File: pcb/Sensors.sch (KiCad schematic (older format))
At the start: 6 parts, among them U1 MPL3115A2, U13 HTS221

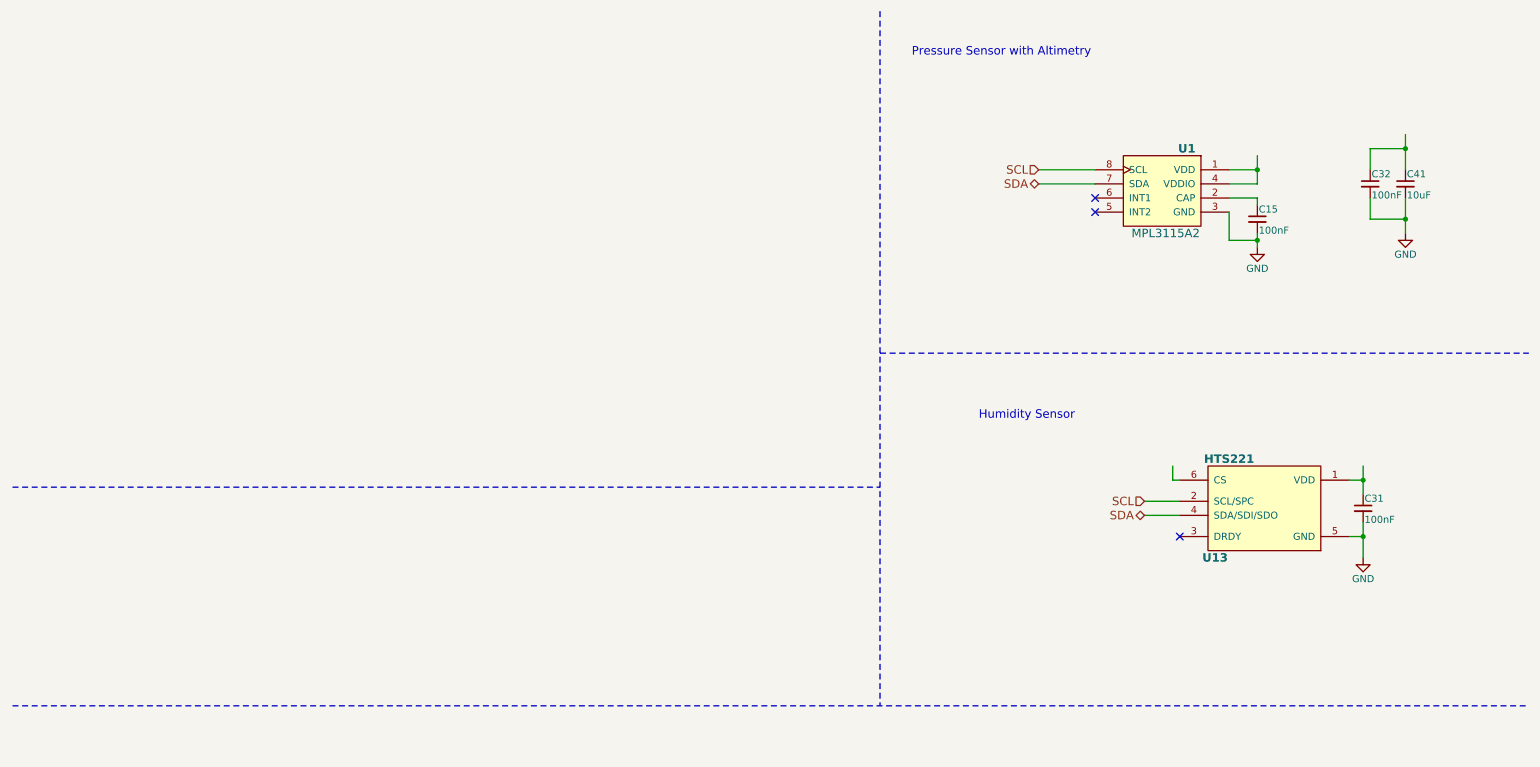
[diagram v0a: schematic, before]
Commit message: sensor array started
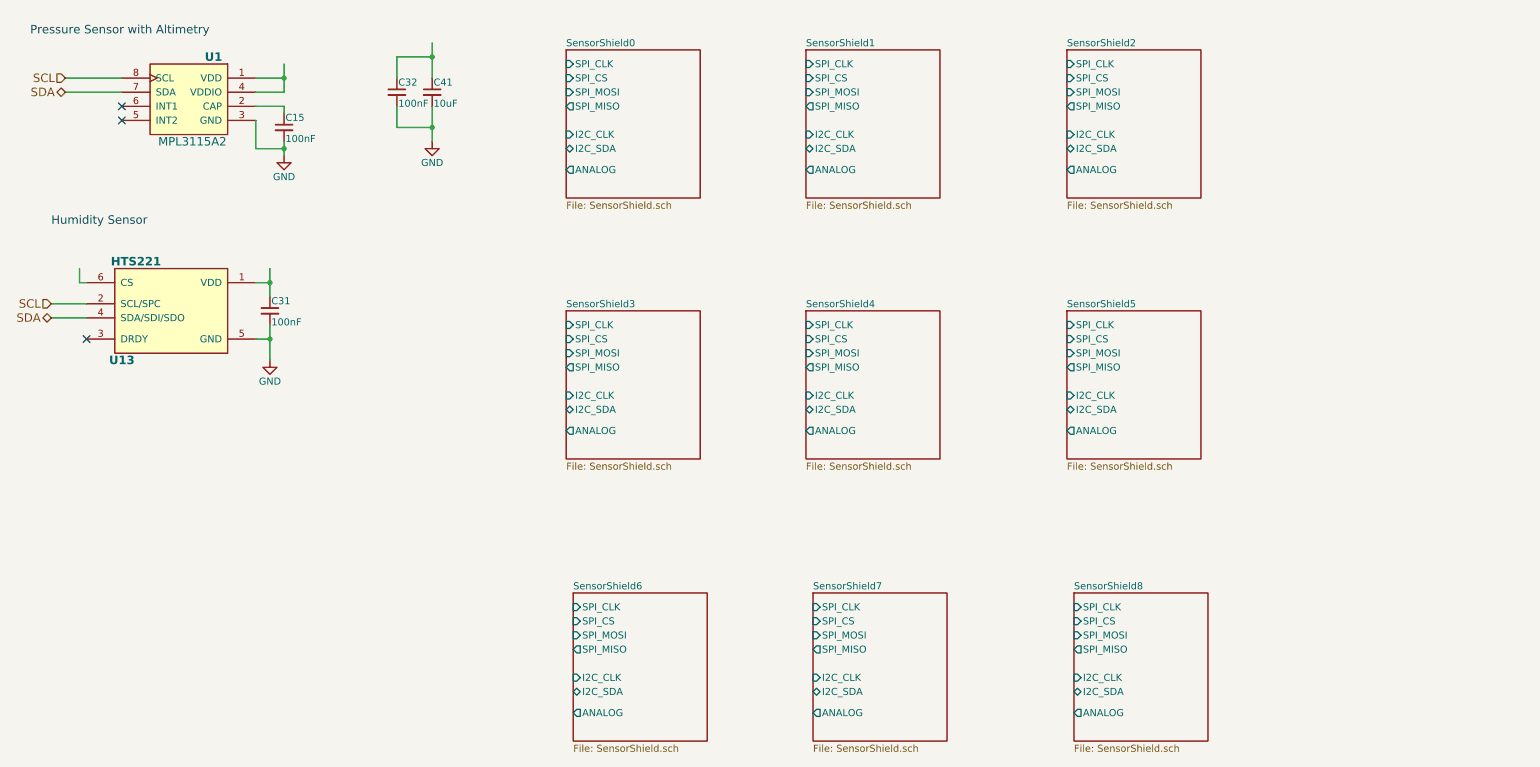
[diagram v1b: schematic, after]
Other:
- moved on the sheet: C15, C31, C32, C41, U1, U13

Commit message: array sensor improved
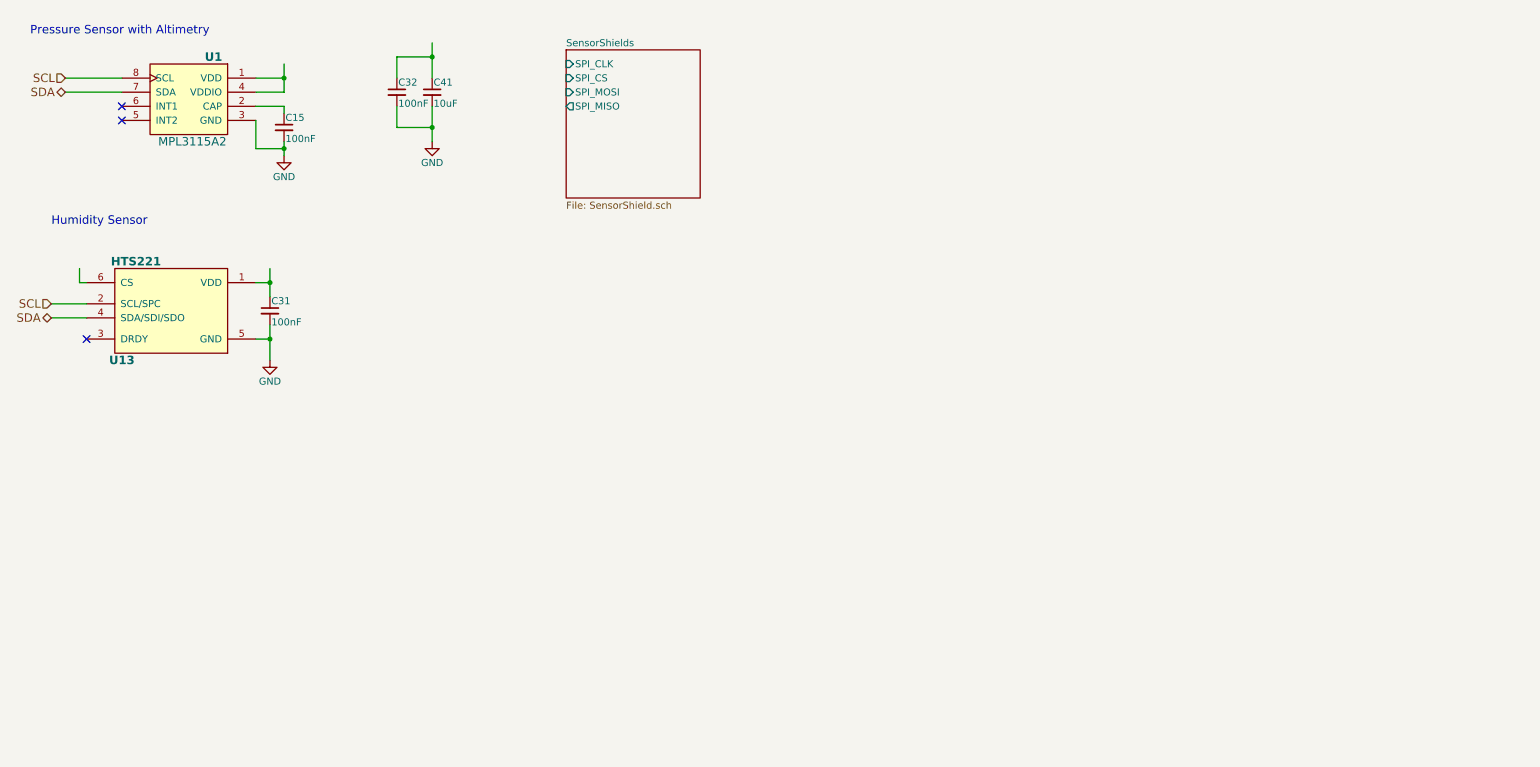
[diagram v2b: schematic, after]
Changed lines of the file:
@@
 $Descr A4 11693 8268
 encoding utf-8
-Sheet 8 18
+Sheet 8 9
 Title "Open  Controller V1.0"
 Date "2020-04-16"
@@
 S 4400 750  950  1050
 U 5E9ECB99
-F0 "SensorShield0" 50
+F0 "SensorShields" 50
 F1 "SensorShield.sch" 50
 F2 "SPI_MISO" O L 4400 1150 50
@@
 F4 "SPI_CS" I L 4400 950 50
 F5 "SPI_CLK" I L 4400 850 50
-F6 "I2C_SDA" B L 4400 1450 50
-F7 "I2C_CLK" I L 4400 1350 50
-F8 "ANALOG" O L 4400 1600 50
-$EndSheet
-$Sheet
-S 6100 750  950  1050
-U 5EA15EEE
-F0 "SensorShield1" 50
-F1 "SensorShield.sch" 50
-F2 "SPI_MISO" O L 6100 1150 50
-F3 "SPI_MOSI" I L 6100 1050 50
-F4 "SPI_CS" I L 6100 950 50
-F5 "SPI_CLK" I L 6100 850 50
-F6 "I2C_SDA" B L 6100 1450 50
-F7 "I2C_CLK" I L 6100 1350 50
-F8 "ANALOG" O L 6100 1600 50
-$EndSheet
-$Sheet
-S 7950 750  950  1050
-U 5EA18277
-F0 "SensorShield2" 50
-F1 "SensorShield.sch" 50
-F2 "SPI_MISO" O L 7950 1150 50
-F3 "SPI_MOSI" I L 7950 1050 50
-F4 "SPI_CS" I L 7950 950 50
-F5 "SPI_CLK" I L 7950 850 50
-F6 "I2C_SDA" B L 7950 1450 50
-F7 "I2C_CLK" I L 7950 1350 50
-F8 "ANALOG" O L 7950 1600 50
-$EndSheet
-$Sheet
-S 4400 2600 950  1050
-U 5EA1A185
-F0 "SensorShield3" 50
-F1 "SensorShield.sch" 50
-F2 "SPI_MISO" O L 4400 3000 50
-F3 "SPI_MOSI" I L 4400 2900 50
-F4 "SPI_CS" I L 4400 2800 50
-F5 "SPI_CLK" I L 4400 2700 50
-F6 "I2C_SDA" B L 4400 3300 50
-F7 "I2C_CLK" I L 4400 3200 50
-F8 "ANALOG" O L 4400 3450 50
-$EndSheet
-$Sheet
-S 6100 2600 950  1050
-U 5EA1A18E
-F0 "SensorShield4" 50
-F1 "SensorShield.sch" 50
-F2 "SPI_MISO" O L 6100 3000 50
-F3 "SPI_MOSI" I L 6100 2900 50
-F4 "SPI_CS" I L 6100 2800 50
-F5 "SPI_CLK" I L 6100 2700 50
-F6 "I2C_SDA" B L 6100 3300 50
-F7 "I2C_CLK" I L 6100 3200 50
-F8 "ANALOG" O L 6100 3450 50
-$EndSheet
-$Sheet
-S 7950 2600 950  1050
-U 5EA1A197
-F0 "SensorShield5" 50
-F1 "SensorShield.sch" 50
-F2 "SPI_MISO" O L 7950 3000 50
-F3 "SPI_MOSI" I L 7950 2900 50
-F4 "SPI_CS" I L 7950 2800 50
-F5 "SPI_CLK" I L 7950 2700 50
-F6 "I2C_SDA" B L 7950 3300 50
-F7 "I2C_CLK" I L 7950 3200 50
-F8 "ANALOG" O L 7950 3450 50
-$EndSheet
-$Sheet
-S 4450 4600 950  1050
-U 5EA1B439
-F0 "SensorShield6" 50
-F1 "SensorShield.sch" 50
-F2 "SPI_MISO" O L 4450 5000 50
-F3 "SPI_MOSI" I L 4450 4900 50
-F4 "SPI_CS" I L 4450 4800 50
-F5 "SPI_CLK" I L 4450 4700 50
-F6 "I2C_SDA" B L 4450 5300 50
-F7 "I2C_CLK" I L 4450 5200 50
-F8 "ANALOG" O L 4450 5450 50
-$EndSheet
-$Sheet
-S 6150 4600 950  1050
-U 5EA1B442
-F0 "SensorShield7" 50
-F1 "SensorShield.sch" 50
-F2 "SPI_MISO" O L 6150 5000 50
-F3 "SPI_MOSI" I L 6150 4900 50
-F4 "SPI_CS" I L 6150 4800 50
-F5 "SPI_CLK" I L 6150 4700 50
-F6 "I2C_SDA" B L 6150 5300 50
-F7 "I2C_CLK" I L 6150 5200 50
-F8 "ANALOG" O L 6150 5450 50
-$EndSheet
-$Sheet
-S 8000 4600 950  1050
-U 5EA1B44B
-F0 "SensorShield8" 50
-F1 "SensorShield.sch" 50
-F2 "SPI_MISO" O L 8000 5000 50
-F3 "SPI_MOSI" I L 8000 4900 50
-F4 "SPI_CS" I L 8000 4800 50
-F5 "SPI_CLK" I L 8000 4700 50
-F6 "I2C_SDA" B L 8000 5300 50
-F7 "I2C_CLK" I L 8000 5200 50
-F8 "ANALOG" O L 8000 5450 50
 $EndSheet
 $EndSCHEMATC

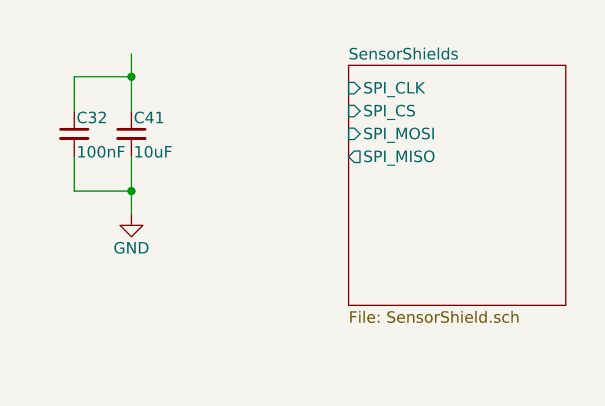
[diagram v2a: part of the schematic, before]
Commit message: array of connectors replacment
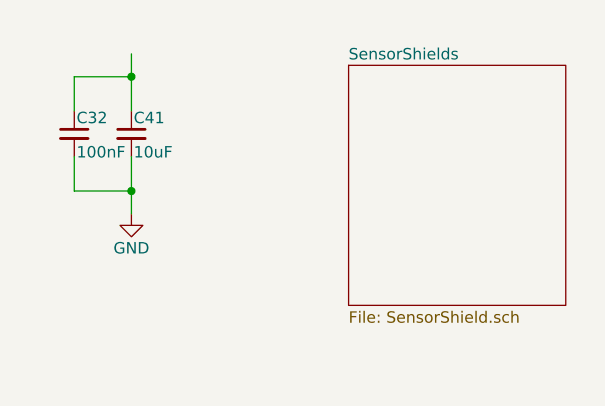
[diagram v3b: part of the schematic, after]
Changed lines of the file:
@@
 F0 "SensorShields" 50
 F1 "SensorShield.sch" 50
-F2 "SPI_MISO" O L 4400 1150 50
-F3 "SPI_MOSI" I L 4400 1050 50
-F4 "SPI_CS" I L 4400 950 50
-F5 "SPI_CLK" I L 4400 850 50
 $EndSheet
 $EndSCHEMATC

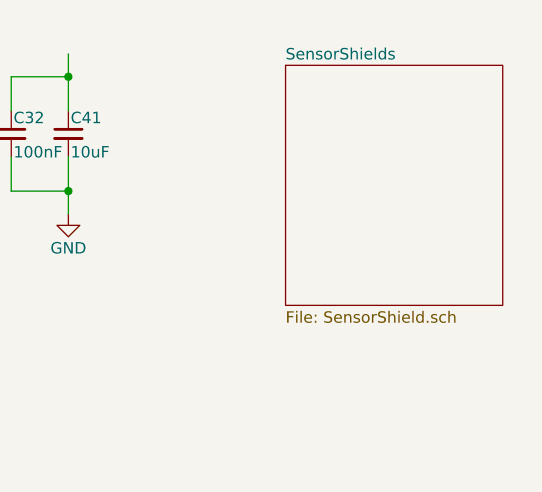
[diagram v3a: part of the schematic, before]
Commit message: schematic simplified
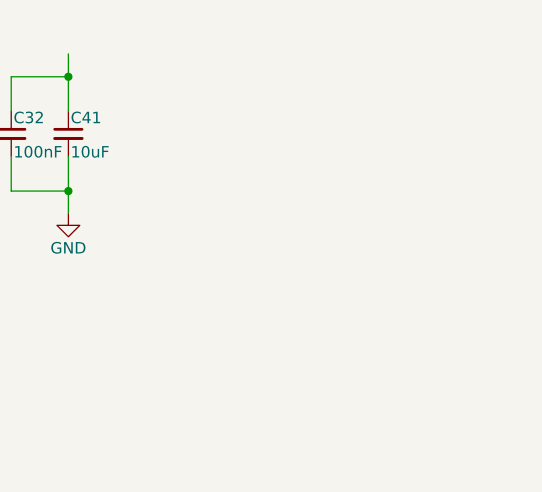
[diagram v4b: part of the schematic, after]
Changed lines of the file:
@@
 Wire Wire Line
 	2400 1450 2400 1500
-$Sheet
-S 4400 750  950  1050
-U 5E9ECB99
-F0 "SensorShields" 50
-F1 "SensorShield.sch" 50
-$EndSheet
 $EndSCHEMATC

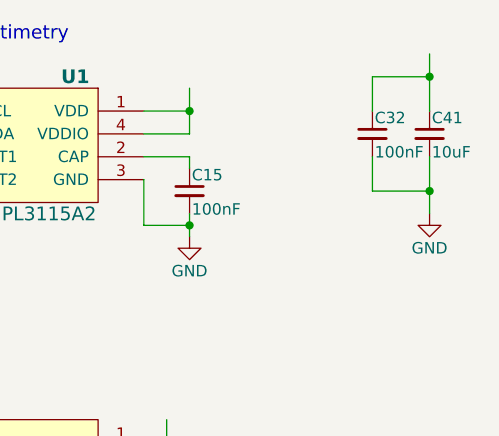
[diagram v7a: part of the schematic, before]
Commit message: rtc placement
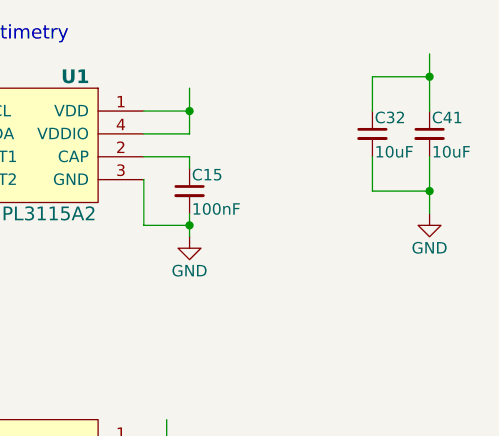
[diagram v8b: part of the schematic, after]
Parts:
- C32: value 100nF -> 10uF; footprint Capacitor_SMD:C_0402_1005Metric -> Capacitor_SMD:C_0603_1608Metric
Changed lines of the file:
@@
 $Descr A4 11693 8268
 encoding utf-8
-Sheet 7 9
+Sheet 5 9
 Title "Open  Controller V1.0"
 Date "2020-04-16"
@@
 P 3200 1050
 F 0 "C32" H 3210 1120 50  0000 L CNN
-F 1 "100nF" H 3210 970 50  0000 L CNN
-F 2 "Capacitor_SMD:C_0402_1005Metric" H 3200 1050 60  0001 C CNN
+F 1 "10uF" H 3210 970 50  0000 L CNN
+F 2 "Capacitor_SMD:C_0603_1608Metric" H 3200 1050 60  0001 C CNN
 F 3 "" H 3200 1050 60  0000 C CNN
 	1    3200 1050
